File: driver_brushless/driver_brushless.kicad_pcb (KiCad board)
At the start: 2 copper layers, 50 x 50 mm, 38 parts, among them U5 L6235D

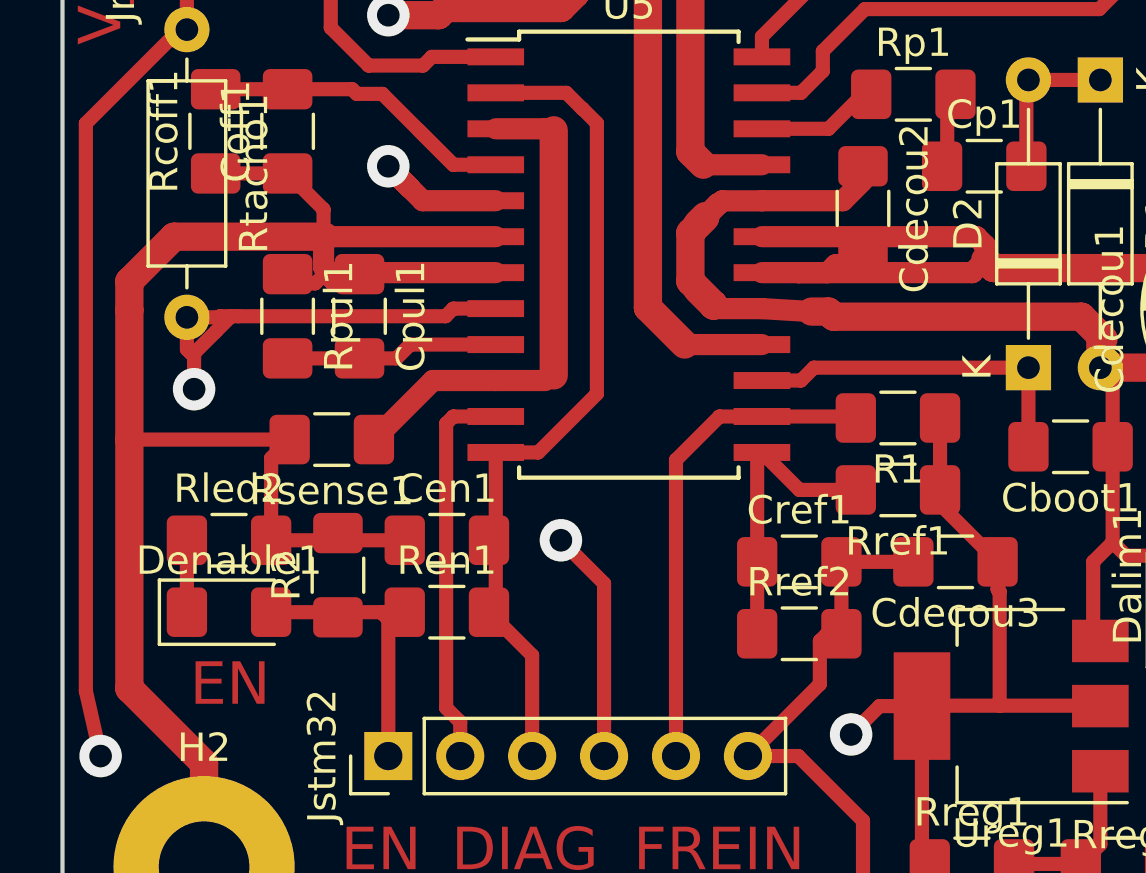
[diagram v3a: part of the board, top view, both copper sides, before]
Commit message: modif du PCB driver_brushless
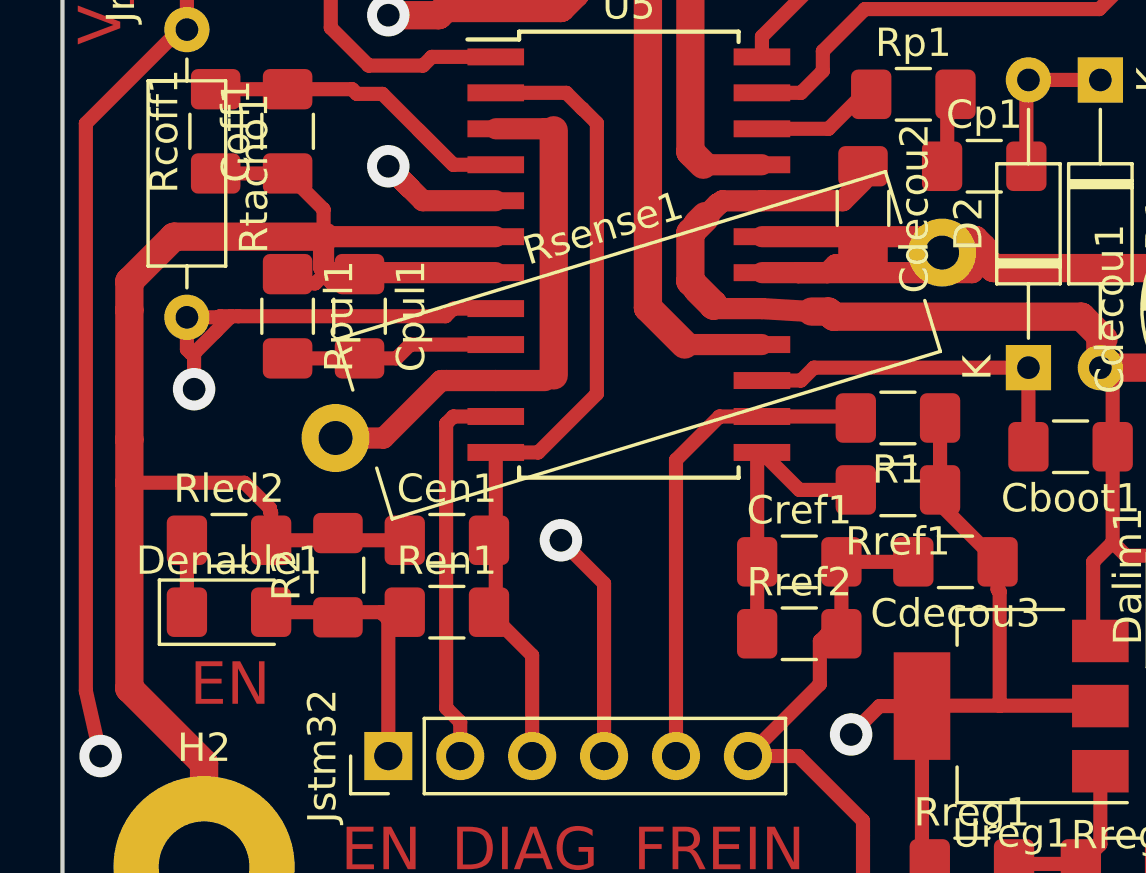
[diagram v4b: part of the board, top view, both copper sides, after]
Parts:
- Rsense1: footprint Resistor_SMD:R_1206_3216Metric_Pad1.42x1.75mm_HandSolder -> Resistor_THT:R_Axial_Power_L20.0mm_W6.4mm_P22.40mm
- moved Rsense1 0.14 mm to (109.6, 89.9), turned to 17 degrees
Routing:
- net GND: track 275.3 -> 272.3 mm
- net Net-(Rsense1-Pad1): track 18.8 -> 20.1 mm
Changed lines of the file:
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@@
     (thickness 1.6)
     (drawings 17)
-    (tracks 288)
+    (tracks 293)
     (zones 0)
     (modules 38)
@@
   )
   (setup
-    (last_trace_width 0.5)
+    (last_trace_width 0.75)
     (user_trace_width 0.75)
     (user_trace_width 1)
@@
     (pad 2 smd roundrect (at 1.4875 0) (size 1.425 1.75) (layers F.Cu F.Paste F.Mask) (roundrect_rratio 0.175439)
       (net 3 GND))
-    (model ${KISYS3DMOD}/Resistor_SMD.3dshapes/R_1206_3216Metric.wrl
-      (at (xyz 0 0 0))
-      (scale (xyz 1 1 1))
-      (rotate (xyz 0 0 0))
-    )
-  )
-  (module Resistor_SMD:R_1206_3216Metric_Pad1.42x1.75mm_HandSolder (layer F.Cu)
-    (at 109.5105 89.916 180)
-    (descr "Resistor SMD 1206 (3216 Metric), square (rectangular) end terminal, IPC_7351 nominal with elongated pad for handsoldering. (Body size source: http://www.tortai-tech.com/upload/download/2011102023233369053.pdf), generated with kicad-footprint-generator")
-    (tags "resistor handsolder")
-    (attr smd)
-    (fp_text reference Rsense1 (at 0 -1.82 180) (layer F.SilkS)
-      (effects (font (size 1 1) (thickness 0.15)))
-    )
-    (fp_text value 0.3 (at 0 1.82 180) (layer F.Fab)
-      (effects (font (size 1 1) (thickness 0.15)))
-    )
-    (fp_text user %R (at 0 0 180) (layer F.Fab)
-      (effects (font (size 0.8 0.8) (thickness 0.12)))
-    )
-    (fp_line (start 2.45 1.12) (end -2.45 1.12) (layer F.CrtYd) (width 0.05))
-    (fp_line (start 2.45 -1.12) (end 2.45 1.12) (layer F.CrtYd) (width 0.05))
-    (fp_line (start -2.45 -1.12) (end 2.45 -1.12) (layer F.CrtYd) (width 0.05))
-    (fp_line (start -2.45 1.12) (end -2.45 -1.12) (layer F.CrtYd) (width 0.05))
-    (fp_line (start -0.602064 0.91) (end 0.602064 0.91) (layer F.SilkS) (width 0.12))
-    (fp_line (start -0.602064 -0.91) (end 0.602064 -0.91) (layer F.SilkS) (width 0.12))
-    (fp_line (start 1.6 0.8) (end -1.6 0.8) (layer F.Fab) (width 0.1))
-    (fp_line (start 1.6 -0.8) (end 1.6 0.8) (layer F.Fab) (width 0.1))
-    (fp_line (start -1.6 -0.8) (end 1.6 -0.8) (layer F.Fab) (width 0.1))
-    (fp_line (start -1.6 0.8) (end -1.6 -0.8) (layer F.Fab) (width 0.1))
-    (pad 2 smd roundrect (at 1.4875 0 180) (size 1.425 1.75) (layers F.Cu F.Paste F.Mask) (roundrect_rratio 0.175439)
-      (net 3 GND))
-    (pad 1 smd roundrect (at -1.4875 0 180) (size 1.425 1.75) (layers F.Cu F.Paste F.Mask) (roundrect_rratio 0.175439)
-      (net 24 "Net-(Rsense1-Pad1)"))
     (model ${KISYS3DMOD}/Resistor_SMD.3dshapes/R_1206_3216Metric.wrl
       (at (xyz 0 0 0))
@@
     )
   )
+  (module Resistor_THT:R_Axial_Power_L20.0mm_W6.4mm_P22.40mm (layer F.Cu)
+    (at 109.642773 89.861126 17)
+    (descr "Resistor, Axial_Power series, Box, pin pitch=22.4mm, 4W, length*width*height=20*6.4*6.4mm^3, http://cdn-reichelt.de/documents/datenblatt/B400/5WAXIAL_9WAXIAL_11WAXIAL_17WAXIAL%23YAG.pdf")
+    (tags "Resistor Axial_Power series Box pin pitch 22.4mm 4W length 20mm width 6.4mm height 6.4mm")
+    (fp_text reference Rsense1 (at 11.2 -4.32 17) (layer F.SilkS)
+      (effects (font (size 1 1) (thickness 0.15)))
+    )
+    (fp_text value 0.3 (at 11.2 4.32 17) (layer F.Fab)
+      (effects (font (size 1 1) (thickness 0.15)))
+    )
+    (fp_line (start 1.2 -3.2) (end 1.2 3.2) (layer F.Fab) (width 0.1))
+    (fp_line (start 1.2 3.2) (end 21.2 3.2) (layer F.Fab) (width 0.1))
+    (fp_line (start 21.2 3.2) (end 21.2 -3.2) (layer F.Fab) (width 0.1))
+    (fp_line (start 21.2 -3.2) (end 1.2 -3.2) (layer F.Fab) (width 0.1))
+    (fp_line (start 0 0) (end 1.2 0) (layer F.Fab) (width 0.1))
+    (fp_line (start 22.4 0) (end 21.2 0) (layer F.Fab) (width 0.1))
+    (fp_line (start 1.08 -1.44) (end 1.08 -3.32) (layer F.SilkS) (width 0.12))
+    (fp_line (start 1.08 -3.32) (end 21.32 -3.32) (layer F.SilkS) (width 0.12))
+    (fp_line (start 21.32 -3.32) (end 21.32 -1.44) (layer F.SilkS) (width 0.12))
+    (fp_line (start 1.08 1.44) (end 1.08 3.32) (layer F.SilkS) (width 0.12))
+    (fp_line (start 1.08 3.32) (end 21.32 3.32) (layer F.SilkS) (width 0.12))
+    (fp_line (start 21.32 3.32) (end 21.32 1.44) (layer F.SilkS) (width 0.12))
+    (fp_line (start -1.45 -3.45) (end -1.45 3.45) (layer F.CrtYd) (width 0.05))
+    (fp_line (start -1.45 3.45) (end 23.85 3.45) (layer F.CrtYd) (width 0.05))
+    (fp_line (start 23.85 3.45) (end 23.85 -3.45) (layer F.CrtYd) (width 0.05))
+    (fp_line (start 23.85 -3.45) (end -1.45 -3.45) (layer F.CrtYd) (width 0.05))
+    (fp_text user %R (at 11.2 0 17) (layer F.Fab)
+      (effects (font (size 1 1) (thickness 0.15)))
+    )
+    (pad 1 thru_hole circle (at 0 0 17) (size 2.4 2.4) (drill 1.2) (layers *.Cu *.Mask)
+      (net 24 "Net-(Rsense1-Pad1)"))
+    (pad 2 thru_hole oval (at 22.4 0 17) (size 2.4 2.4) (drill 1.2) (layers *.Cu *.Mask)
+      (net 3 GND))
+    (model ${KISYS3DMOD}/Resistor_THT.3dshapes/R_Axial_Power_L20.0mm_W6.4mm_P22.40mm.wrl
+      (at (xyz 0 0 0))
+      (scale (xyz 1 1 1))
+      (rotate (xyz 0 0 0))
+    )
+  )
   (gr_text Alim (at 139.446 90.424 90) (layer F.Cu)
     (effects (font (size 1.3 1.3) (thickness 0.3)))
@@
   (segment (start 108.92499 108.92499) (end 128.27 108.92499) (width 1) (layer F.Cu) (net 3))
   (segment (start 128.27 103.886) (end 128.27 108.92499) (width 0.5) (layer F.Cu) (net 3))
-  (segment (start 107.369 90.57) (end 108.023 89.916) (width 0.5) (layer F.Cu) (net 3))
-  (segment (start 107.369 93.472) (end 107.369 90.57) (width 0.5) (layer F.Cu) (net 3))
-  (segment (start 108.023 89.916) (end 102.362 89.916) (width 0.5) (layer F.Cu) (net 3))
   (segment (start 114.554 71.882) (end 114.554 68.834) (width 0.5) (layer F.Cu) (net 3))
   (segment (start 114.554 69.088) (end 114.554 68.834) (width 0.5) (layer F.Cu) (net 3))
@@
   (segment (start 105 101.346) (end 105 105) (width 1) (layer F.Cu) (net 3))
   (segment (start 102.362 98.708) (end 105 101.346) (width 1) (layer F.Cu) (net 3))
-  (segment (start 102.362 89.916) (end 102.362 98.708) (width 1) (layer F.Cu) (net 3))
   (segment (start 102.362 84.328) (end 102.362 85.344) (width 1) (layer F.Cu) (net 3))
   (segment (start 102.362 85.344) (end 102.362 89.916) (width 1) (layer F.Cu) (net 3))
@@
   (segment (start 138.938 74.93) (end 138.938 82.804) (width 1) (layer F.Cu) (net 3))
   (segment (start 138.938 82.804) (end 138.938 83.606) (width 1) (layer F.Cu) (net 3))
+  (segment (start 107.369 92.497) (end 107.328 92.456) (width 0.5) (layer F.Cu) (net 3))
+  (segment (start 107.369 93.472) (end 107.369 92.497) (width 0.5) (layer F.Cu) (net 3))
+  (segment (start 107.328 92.456) (end 107.328 92.342) (width 0.5) (layer F.Cu) (net 3))
+  (segment (start 106.426 91.44) (end 102.362 91.44) (width 0.5) (layer F.Cu) (net 3))
+  (segment (start 107.328 92.342) (end 106.426 91.44) (width 0.5) (layer F.Cu) (net 3))
+  (segment (start 102.362 89.916) (end 102.362 91.44) (width 1) (layer F.Cu) (net 3))
+  (segment (start 102.362 91.44) (end 102.362 98.708) (width 1) (layer F.Cu) (net 3))
   (segment (start 130.991 89.154) (end 130.991 91.694) (width 0.5) (layer F.Cu) (net 4))
   (segment (start 130.991 92.202) (end 133.023 94.234) (width 0.5) (layer F.Cu) (net 4))
@@
   (segment (start 115.301001 87.831001) (end 117.051001 87.831001) (width 0.75) (layer F.Cu) (net 24))
   (segment (start 117.348 78.994) (end 117.348 87.65) (width 1) (layer F.Cu) (net 24))
-  (segment (start 113.082999 87.831001) (end 110.998 89.916) (width 0.75) (layer F.Cu) (net 24))
-  (segment (start 115.301001 87.831001) (end 113.082999 87.831001) (width 0.75) (layer F.Cu) (net 24))
+  (segment (start 113.551001 87.831001) (end 115.301001 87.831001) (width 0.75) (layer F.Cu) (net 24))
+  (segment (start 113.369954 87.831001) (end 113.551001 87.831001) (width 0.75) (layer F.Cu) (net 24))
+  (segment (start 111.339829 89.861126) (end 113.369954 87.831001) (width 0.75) (layer F.Cu) (net 24))
+  (segment (start 109.642773 89.861126) (end 111.339829 89.861126) (width 0.75) (layer F.Cu) (net 24))
   (segment (start 145.796 78.486) (end 144.78 77.47) (width 1) (layer F.Cu) (net 25))
   (segment (start 145.796 92.71) (end 145.796 91.694) (width 1) (layer F.Cu) (net 25))

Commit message: afficheGrapheSerie
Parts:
- Ureg1: value LM317_3PinPackage -> LM317
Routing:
- net Net-(Cen1-Pad2): track 30.9 -> 32.6 mm
- net /Out_21: track 17.5 -> 19.1 mm
- net Net-(Rsense1-Pad1): track 20.1 -> 21.5 mm
- net /Out_31: track 23.4 -> 24.6 mm
